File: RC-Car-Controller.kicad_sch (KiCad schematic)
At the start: 0 parts

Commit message: Update placement
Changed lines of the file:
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@@
     (title "RamyMawal-18-09-2023")
   )
-  (text "Motor Drivers" (at 643.89 67.31 0)
+  (text "Motor Drivers" (at 353.06 234.95 0)
     (effects (font (size 12 12)) (justify left bottom))
   )
-  (text "Sensors" (at 67.31 283.21 0)
+  (text "Sensors" (at 106.68 237.49 0)
     (effects (font (size 12 12)) (justify left bottom))
   )
-  (text "Controller\n" (at 259.08 90.17 0)
+  (text "Controller\n" (at 400.05 57.15 0)
     (effects (font (size 12 12)) (justify left bottom))
   )
-  (text "Connectors" (at 39.37 30.48 0)
+  (text "Connectors" (at 231.14 58.42 0)
     (effects (font (size 12 12)) (justify left bottom))
   )
-  (text "Power" (at 72.39 158.75 0)
+  (text "Power" (at 78.74 57.15 0)
     (effects (font (size 12 12)) (justify left bottom))
   )
-  (sheet (at 25.4 166.37) (size 149.86 87.63) (fields_autoplaced)
+  (sheet (at 27.94 64.77) (size 149.86 87.63) (fields_autoplaced)
     (stroke (width 0.1524) (type solid))
     (fill (color 0 0 0 0.0000))
-    (property "Sheetname" "Power" (at 25.4 165.6584 0)
+    (property "Sheetname" "Power" (at 27.94 64.0584 0)
       (effects (font (size 1.27 1.27)) (justify left bottom))
     )
-    (property "Sheetfile" "power.kicad_sch" (at 25.4 254.5846 0)
+    (property "Sheetfile" "power.kicad_sch" (at 27.94 152.9846 0)
       (effects (font (size 1.27 1.27)) (justify left top))
     )
-    (property "Field2" "" (at 25.4 166.37 0)
+    (property "Field2" "" (at 27.94 64.77 0)
       (effects (font (size 1.27 1.27)) hide)
     )
@@
     )
   )
-  (sheet (at 30.48 35.56) (size 125.73 74.93) (fields_autoplaced)
+  (sheet (at 222.25 63.5) (size 125.73 74.93) (fields_autoplaced)
     (stroke (width 0.1524) (type solid))
     (fill (color 0 0 0 0.0000))
-    (property "Sheetname" "Connectors" (at 30.48 34.8484 0)
+    (property "Sheetname" "Connectors" (at 222.25 62.7884 0)
       (effects (font (size 1.27 1.27)) (justify left bottom))
     )
-    (property "Sheetfile" "connectors.kicad_sch" (at 30.48 111.0746 0)
+    (property "Sheetfile" "connectors.kicad_sch" (at 222.25 139.0146 0)
       (effects (font (size 1.27 1.27)) (justify left top))
     )
-    (property "Field2" "" (at 30.48 35.56 0)
+    (property "Field2" "" (at 222.25 63.5 0)
       (effects (font (size 1.27 1.27)) hide)
     )
@@
     )
   )
-  (sheet (at 236.22 99.06) (size 129.54 69.85) (fields_autoplaced)
+  (sheet (at 377.19 66.04) (size 129.54 69.85) (fields_autoplaced)
     (stroke (width 0.1524) (type solid))
     (fill (color 0 0 0 0.0000))
-    (property "Sheetname" "ESP32-S3 Microcontroller " (at 236.22 98.3484 0)
+    (property "Sheetname" "ESP32-S3 Microcontroller " (at 377.19 65.3284 0)
       (effects (font (size 1.27 1.27)) (justify left bottom))
     )
-    (property "Sheetfile" "ESP32_S3_MCU.kicad_sch" (at 236.22 169.4946 0)
+    (property "Sheetfile" "ESP32_S3_MCU.kicad_sch" (at 377.19 136.4746 0)
       (effects (font (size 1.27 1.27)) (justify left top))
     )
-    (property "Field2" "" (at 236.22 99.06 0)
+    (property "Field2" "" (at 377.19 66.04 0)
       (effects (font (size 1.27 1.27)) hide)
     )
@@
     )
   )
-  (sheet (at 25.4 289.56) (size 151.13 85.09) (fields_autoplaced)
+  (sheet (at 64.77 243.84) (size 151.13 85.09) (fields_autoplaced)
     (stroke (width 0.1524) (type solid))
     (fill (color 0 0 0 0.0000))
-    (property "Sheetname" "Sensors" (at 25.4 288.8484 0)
+    (property "Sheetname" "Sensors" (at 64.77 243.1284 0)
       (effects (font (size 1.27 1.27)) (justify left bottom))
     )
-    (property "Sheetfile" "sensors.kicad_sch" (at 25.4 375.2346 0)
+    (property "Sheetfile" "sensors.kicad_sch" (at 64.77 329.5146 0)
       (effects (font (size 1.27 1.27)) (justify left top))
     )
-    (property "Field2" "" (at 25.4 289.56 0)
+    (property "Field2" "" (at 64.77 243.84 0)
       (effects (font (size 1.27 1.27)) hide)
     )
@@
     )
   )
-  (sheet (at 632.46 137.16) (size 101.6 71.12) (fields_autoplaced)
+  (sheet (at 356.87 259.08) (size 101.6 71.12) (fields_autoplaced)
     (stroke (width 0.1524) (type solid))
     (fill (color 0 0 0 0.0000))
-    (property "Sheetname" "Motors" (at 632.46 136.4484 0)
+    (property "Sheetname" "Motors" (at 356.87 258.3684 0)
       (effects (font (size 1.27 1.27)) (justify left bottom))
     )
-    (property "Sheetfile" "motors.kicad_sch" (at 632.46 208.8646 0)
+    (property "Sheetfile" "motors.kicad_sch" (at 356.87 330.7846 0)
       (effects (font (size 1.27 1.27)) (justify left top))
     )
-    (property "Field2" "" (at 632.46 137.16 0)
+    (property "Field2" "" (at 356.87 259.08 0)
       (effects (font (size 1.27 1.27)) hide)
     )

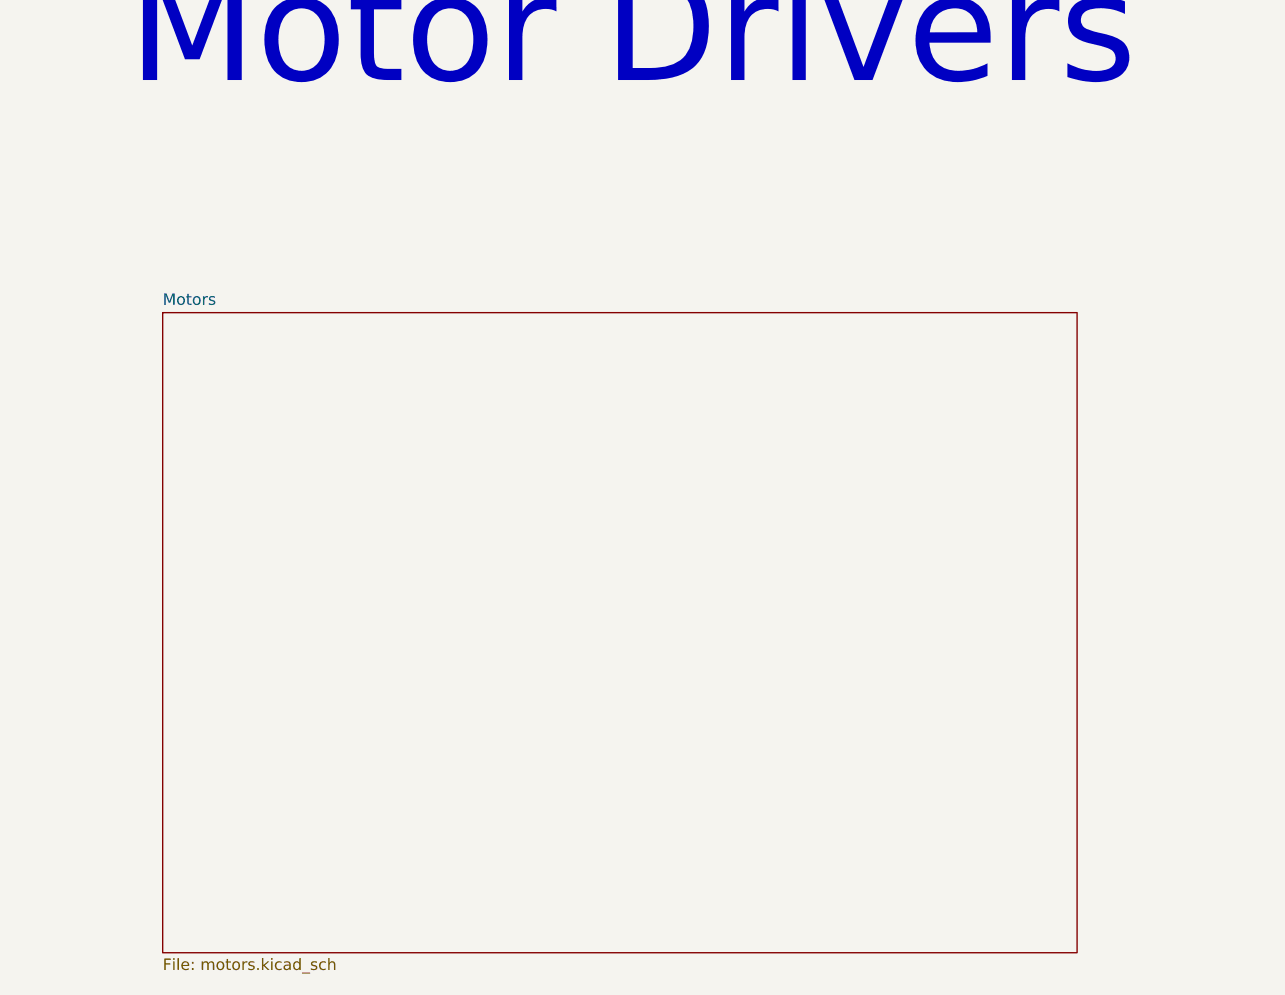
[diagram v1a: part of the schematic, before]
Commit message: Add MPU6050 and LIS2MDL
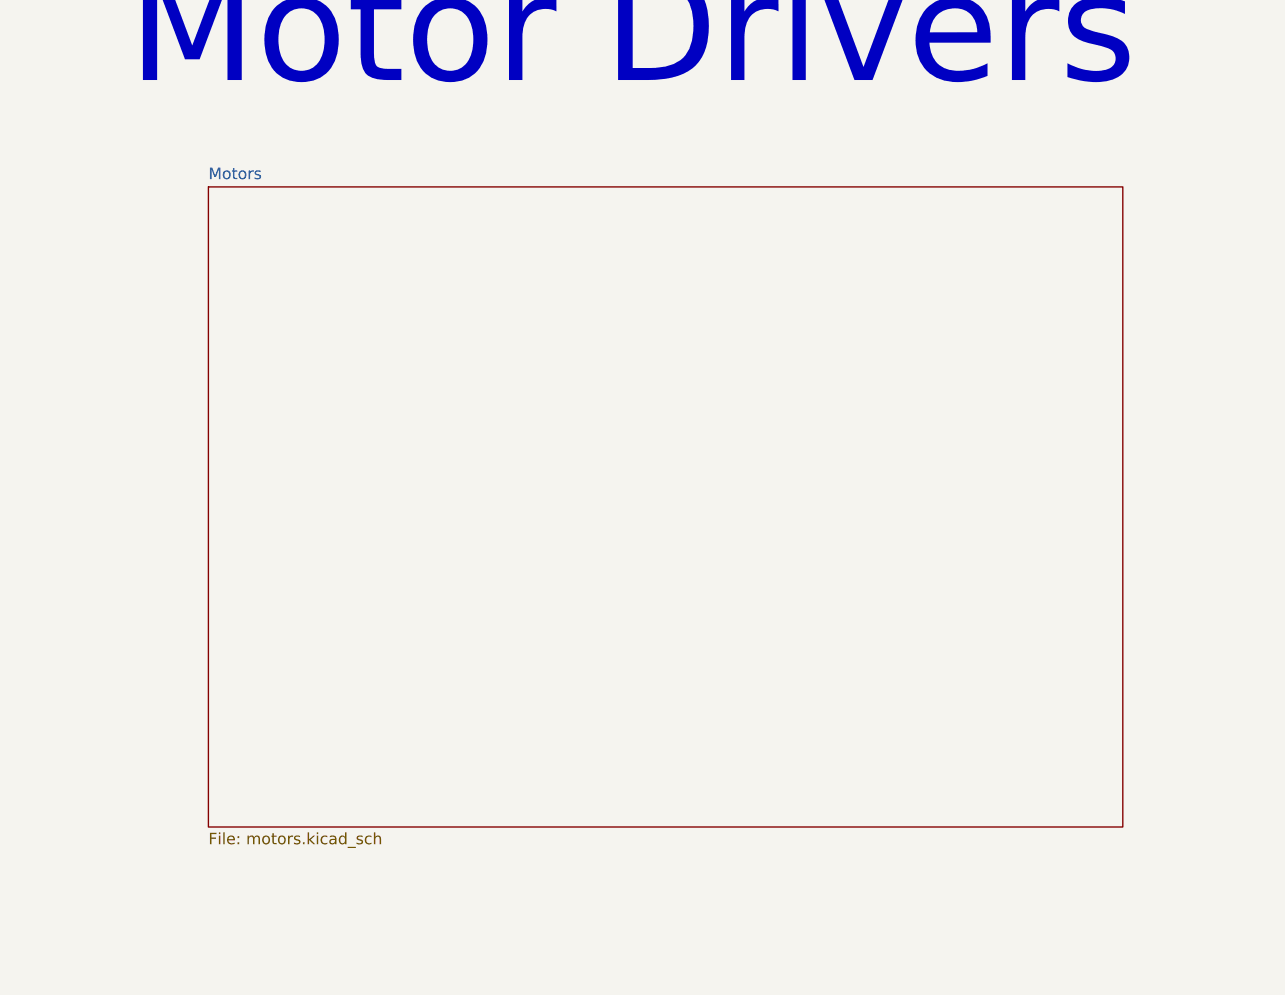
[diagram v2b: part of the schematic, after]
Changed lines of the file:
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@@
     )
   )
-  (sheet (at 356.87 259.08) (size 101.6 71.12) (fields_autoplaced)
+  (sheet (at 361.95 245.11) (size 101.6 71.12) (fields_autoplaced)
     (stroke (width 0.1524) (type solid))
     (fill (color 0 0 0 0.0000))
-    (property "Sheetname" "Motors" (at 356.87 258.3684 0)
+    (property "Sheetname" "Motors" (at 361.95 244.3984 0)
       (effects (font (size 1.27 1.27)) (justify left bottom))
     )
-    (property "Sheetfile" "motors.kicad_sch" (at 356.87 330.7846 0)
+    (property "Sheetfile" "motors.kicad_sch" (at 361.95 316.8146 0)
       (effects (font (size 1.27 1.27)) (justify left top))
     )
-    (property "Field2" "" (at 356.87 259.08 0)
+    (property "Field2" "" (at 361.95 245.11 0)
       (effects (font (size 1.27 1.27)) hide)
     )
